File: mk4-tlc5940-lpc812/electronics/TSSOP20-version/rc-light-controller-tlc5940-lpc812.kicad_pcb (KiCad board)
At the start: 2 copper layers, 27 x 18 mm, 37 parts, among them T1 NMOSSOT23, U1 3V3, U2 LPC812M101JDH20, U3 TLC5940PWP

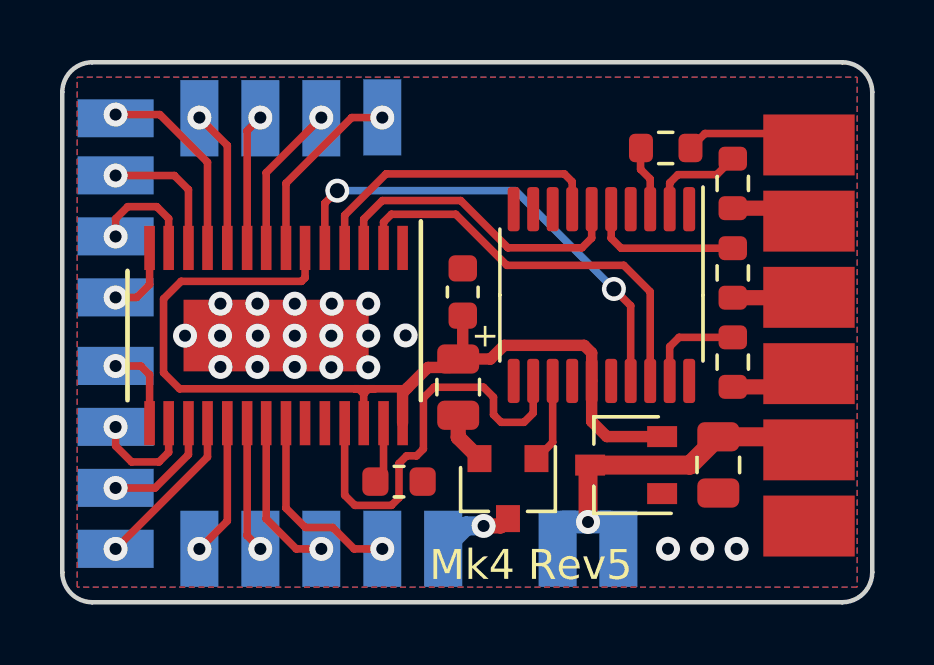
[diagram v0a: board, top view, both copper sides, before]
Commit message: Fix via size and improve ground stitching
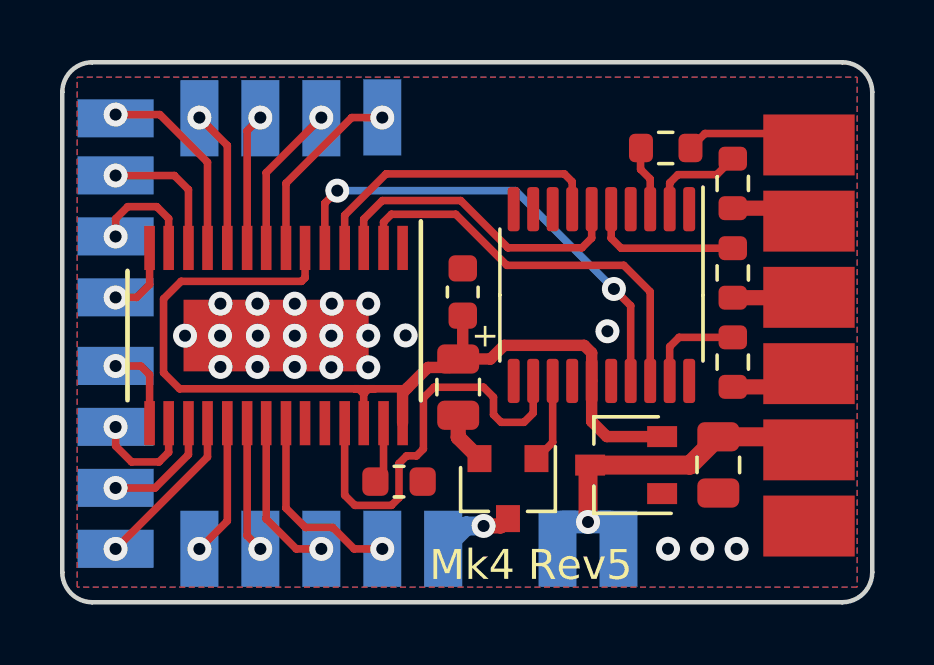
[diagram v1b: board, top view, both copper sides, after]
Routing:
- net GND: vias 20 -> 21
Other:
- net class Default: via_drill 0.5 -> 0.4
